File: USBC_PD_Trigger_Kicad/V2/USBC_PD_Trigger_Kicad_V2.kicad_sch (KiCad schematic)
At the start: 36 parts, among them J1 USB_C_Receptacle_PowerOnly_6P, J2 Screw_Terminal_01x02, SW2 SW_Push, U1 FUSB302BMPX, U3 LS2406ERQ23, U4 ATtiny816-S, U5 AP7375-33SA-7

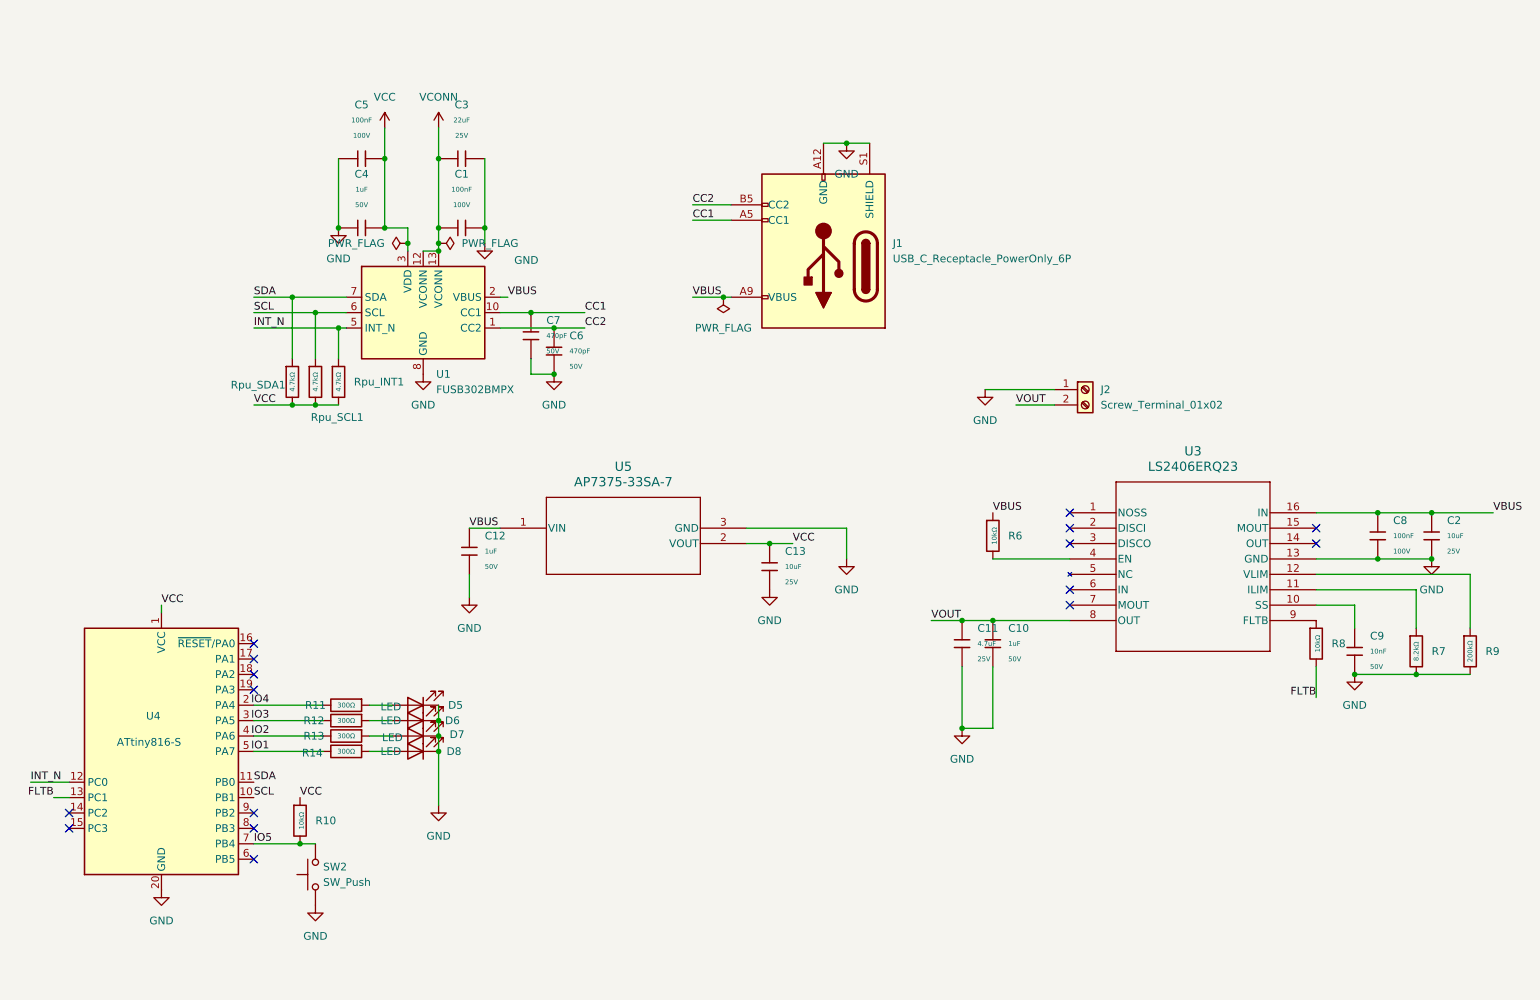
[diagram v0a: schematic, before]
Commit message: Updated Pd trigger to use only 1 cable
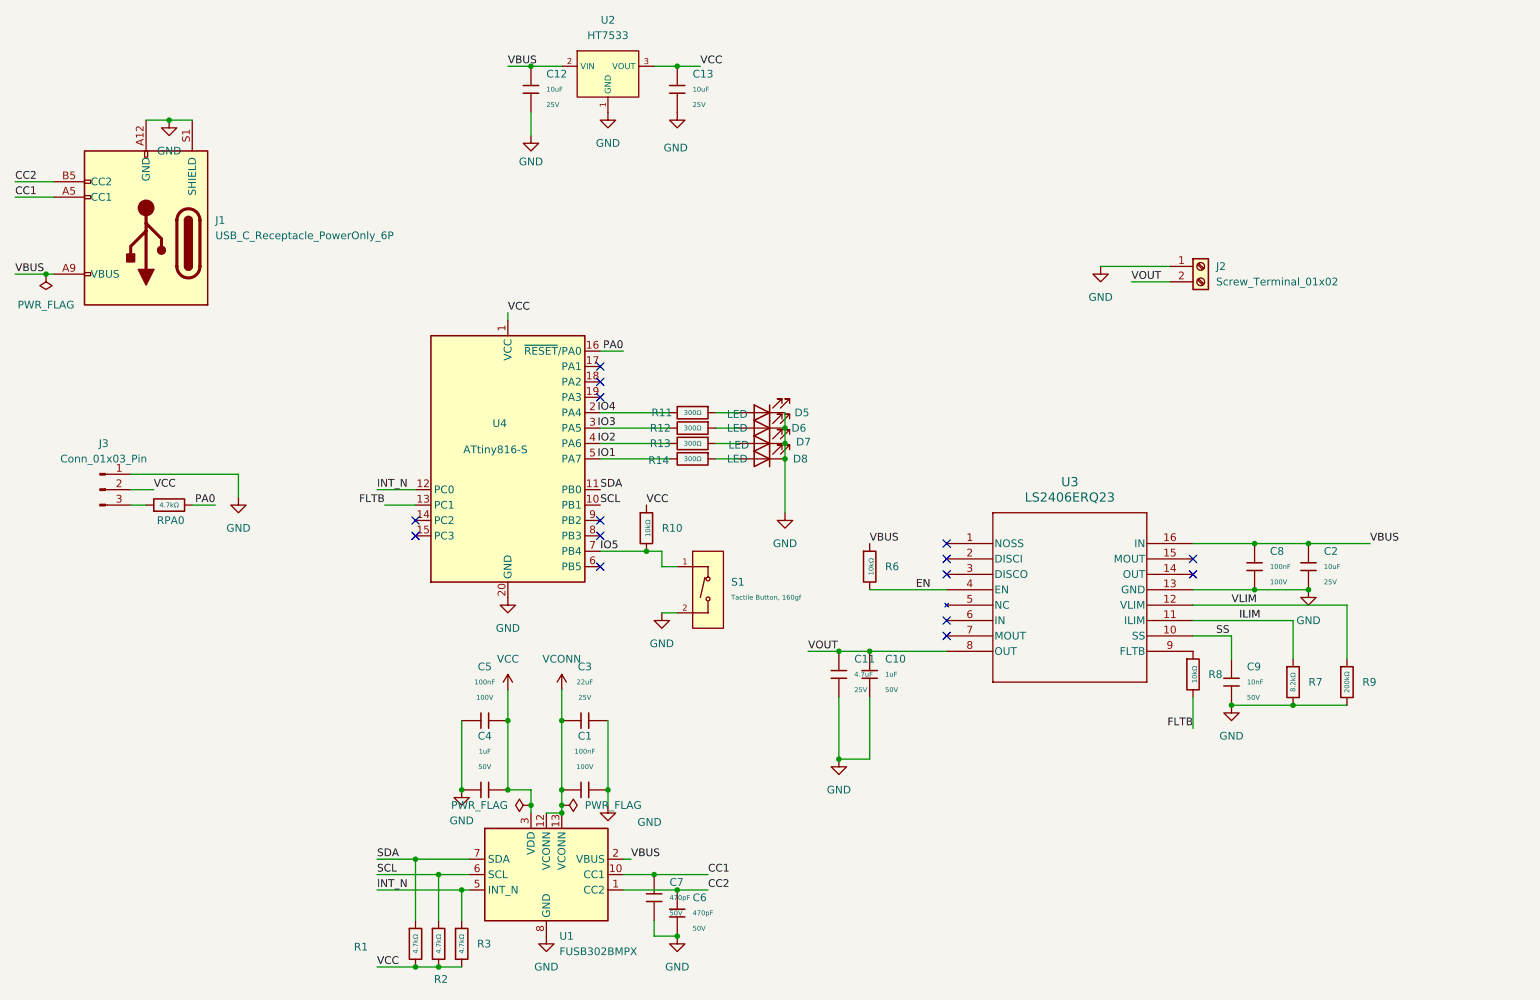
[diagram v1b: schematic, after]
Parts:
- removed C12: 1uF, PCM_JLCPCB:C_0805, symbol PCM_JLCPCB-Capacitors:0805,1uF
- removed SW2: SW_Push, Button_Switch_SMD:SW_SPST_PTS645, symbol Switch:SW_Push
- removed U5: AP7375-33SA-7, AP737:AP7375-33SA-7_DIO, symbol 2026-02-28_01-03-38:AP7375-33SA-7
- added C12: 10uF, PCM_JLCPCB:C_0805, symbol PCM_JLCPCB-Capacitors:0805,10uF
- added J3: Conn_01x03_Pin, Connector_PinHeader_2.54mm:PinHeader_1x03_P2.54mm_Vertical, symbol Connector:Conn_01x03_Pin
- added RPA0: 4.7kΩ, PCM_JLCPCB:R_0805, symbol PCM_JLCPCB-Resistors:0805,4.7kΩ
- added S1: Tactile Button, 160gf, PCM_JLCPCB:SW_TS-1088-AR02016, symbol PCM_JLCPCB-Connectors_Buttons:Tactile Button, 160gf, 12V, 50mA, 4.0mm
- added U2: HT7533, PCM_JLCPCB:SOT-89-3_L4.5-W2.5-P1.50-LS4.2-BR, symbol PCM_JLCPCB-Power:LDO, 3.3V, 0.1A
- renumbered Rpu_SDA1 to R1, Rpu_SCL1 to R2, Rpu_INT1 to R3
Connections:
- net GND: now also C12.2, J3.1 (Pin_1), S1.2 (B), U2.1 (GND)
- net IO5: now also S1.1 (A)
- net VBUS: now also C12.1, U2.2 (VIN)
- net VCC: now also J3.2 (Pin_2), U2.3 (VOUT)
- net VLIM: now reaches R9.1, U3.12 (VLIM)
- net ILIM: now reaches R7.1, U3.11 (ILIM)
- net SS: now reaches C9.1, U3.10 (SS)
- net EN: now reaches R6.2, U3.4 (EN)
- net PA0: now reaches U4.16 (~{RESET}/PA0)
- net PA0: now also RPA0.2
- new net: J3.3 (Pin_3), RPA0.1
- no-connect marks 16 -> 15
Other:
- moved on the sheet: C1, C10, C11, C13, C2, C3, C4, C5, C6, C7, C8, C9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
